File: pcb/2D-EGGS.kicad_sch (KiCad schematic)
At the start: 55 parts, among them J1 ISP, J10 B10, J11 B8, J12 PWAN_CENTER_LED, J13 PWAN_E1P1, J14 PWAN_E1P2, J15 ENCODER1, J16 DPWR, J17 PWAN_E2P1, J18 PWAN_E2P2, J19 ENCODER2, J2 TT_LED, J20 B9, J21 B11, J22 PWAN_USB_B, J23 PWAN_USB_C, J24 LED1, J25 LED2, J26 APWR, J3 B1, J4 B6, J5 B3, J6 B4, J7 B5, J8 B2, J9 B7, P1 USB_C_DATA, P2 USB_C_POWER, Q10 2N7002, Q11 2N7002, Q12 2N7002, Q13 2N7002, Q3 2N7002, Q4 2N7002, Q5 2N7002, Q6 2N7002, Q7 2N7002, Q8 2N7002, Q9 2N7002, SW1 SW_Push, U1 AT90USB1286, Y1 16MHz

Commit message: v3 routed
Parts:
- removed P1: USB_C_DATA, Connector_USB:USB_C_Receptacle_GCT_USB4085, symbol Connector:USB_C_Plug
- removed P2: USB_C_POWER, Connector_USB:USB_C_Receptacle_GCT_USB4085, symbol Connector:USB_C_Plug
- added J27: USB_DATA, Connector_JST:JST_XH_B4B-XH-A_1x04_P2.50mm_Vertical, symbol Connector_Generic:Conn_01x04
- added J28: USB_AUX, Connector_JST:JST_XH_B4B-XH-A_1x04_P2.50mm_Vertical, symbol Connector_Generic:Conn_01x04
- J1: footprint Connector_PinHeader_2.54mm:PinHeader_2x03_P2.54mm_Vertical -> Connector_IDC:IDC-Header_2x03_P2.54mm_Vertical
- J12: value PWAN_CENTER_LED -> DAO_BAR
- J13: value PWAN_E1P1 -> DAO_E1P1
- J14: value PWAN_E1P2 -> DAO_E1P2
- J17: value PWAN_E2P1 -> DAO_E2P1
- J18: value PWAN_E2P2 -> DAO_E2P2
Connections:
- net +5V: now also J27.4 (Pin_4); no longer J12.2 (Pin_2), J2.2 (Pin_2), J23.2 (Pin_2), J24.2 (Pin_2), J25.2 (Pin_2), J26.1 (Pin_1)
- net GND: now also J27.1 (Pin_1), J28.1 (Pin_1)
- net USB-R_D+: now also J27.2 (Pin_2)
- net USB-R_D-: now also J27.3 (Pin_3)
- new net +5VA: J12.2 (Pin_2), J2.2 (Pin_2), J23.2 (Pin_2), J24.2 (Pin_2), J25.2 (Pin_2), J26.1 (Pin_1), J28.4 (Pin_4)
- no-connect marks 43 -> 19

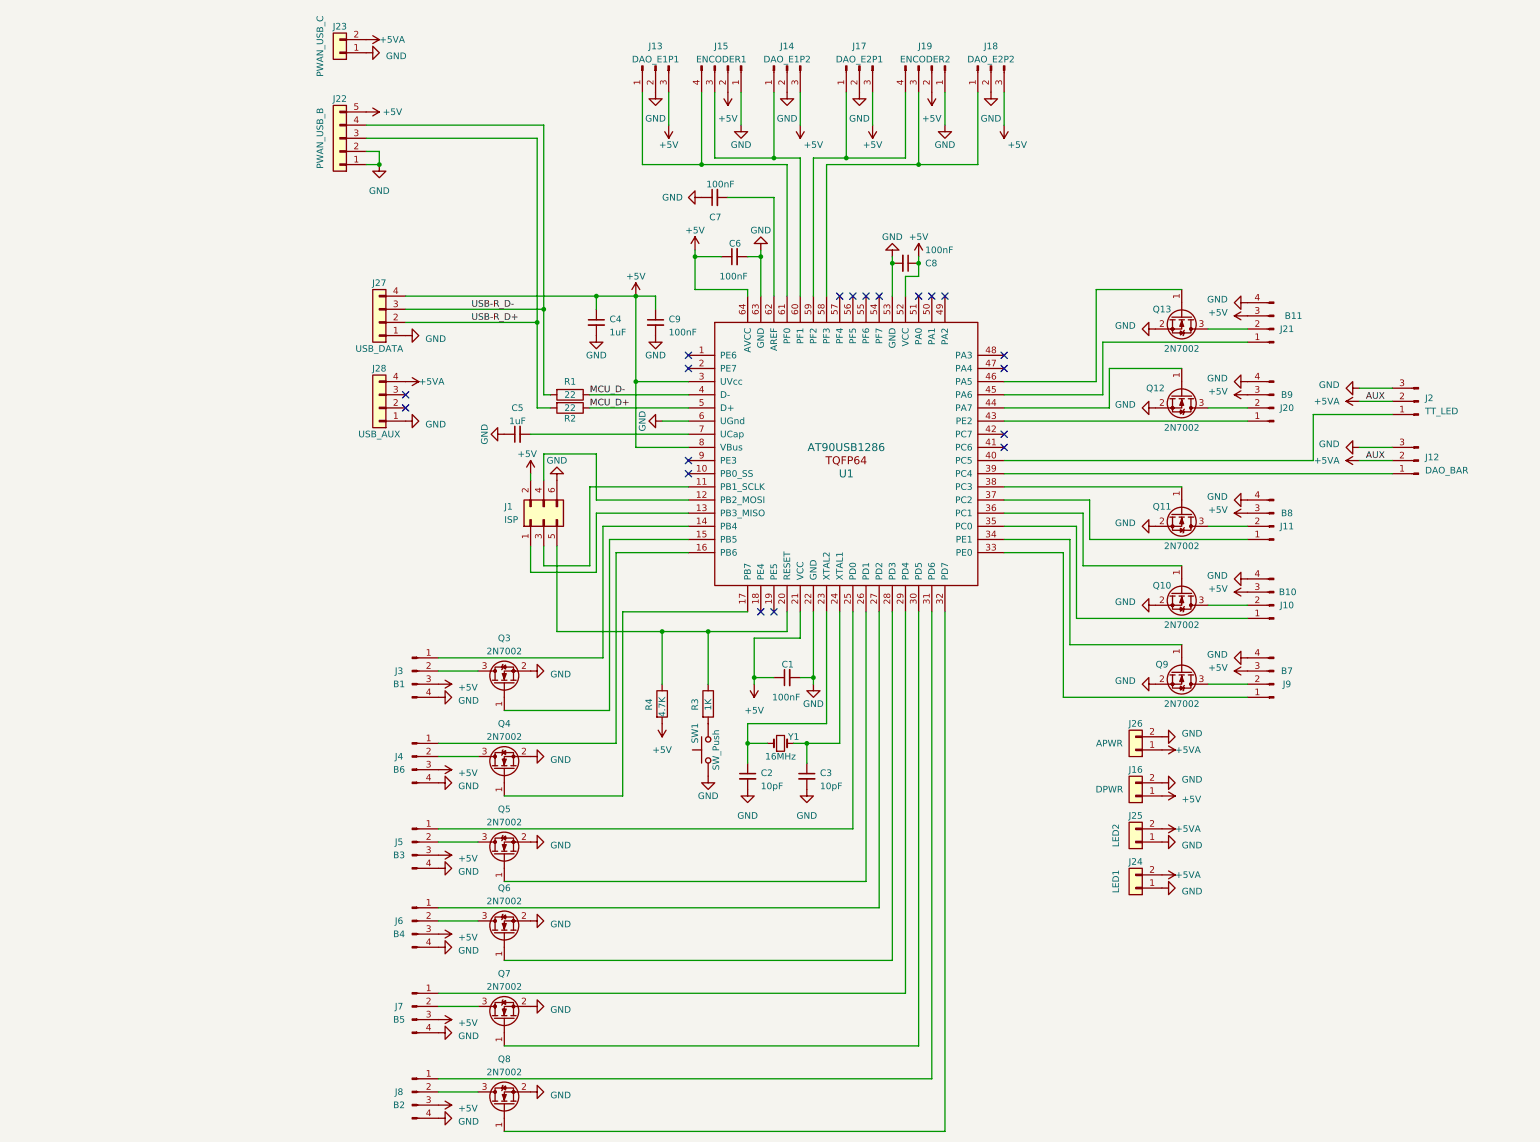
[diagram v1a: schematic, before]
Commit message: finalize V3
reduced JST-XH holes from 0.95mm -> 0.9mm, minor changes to layout
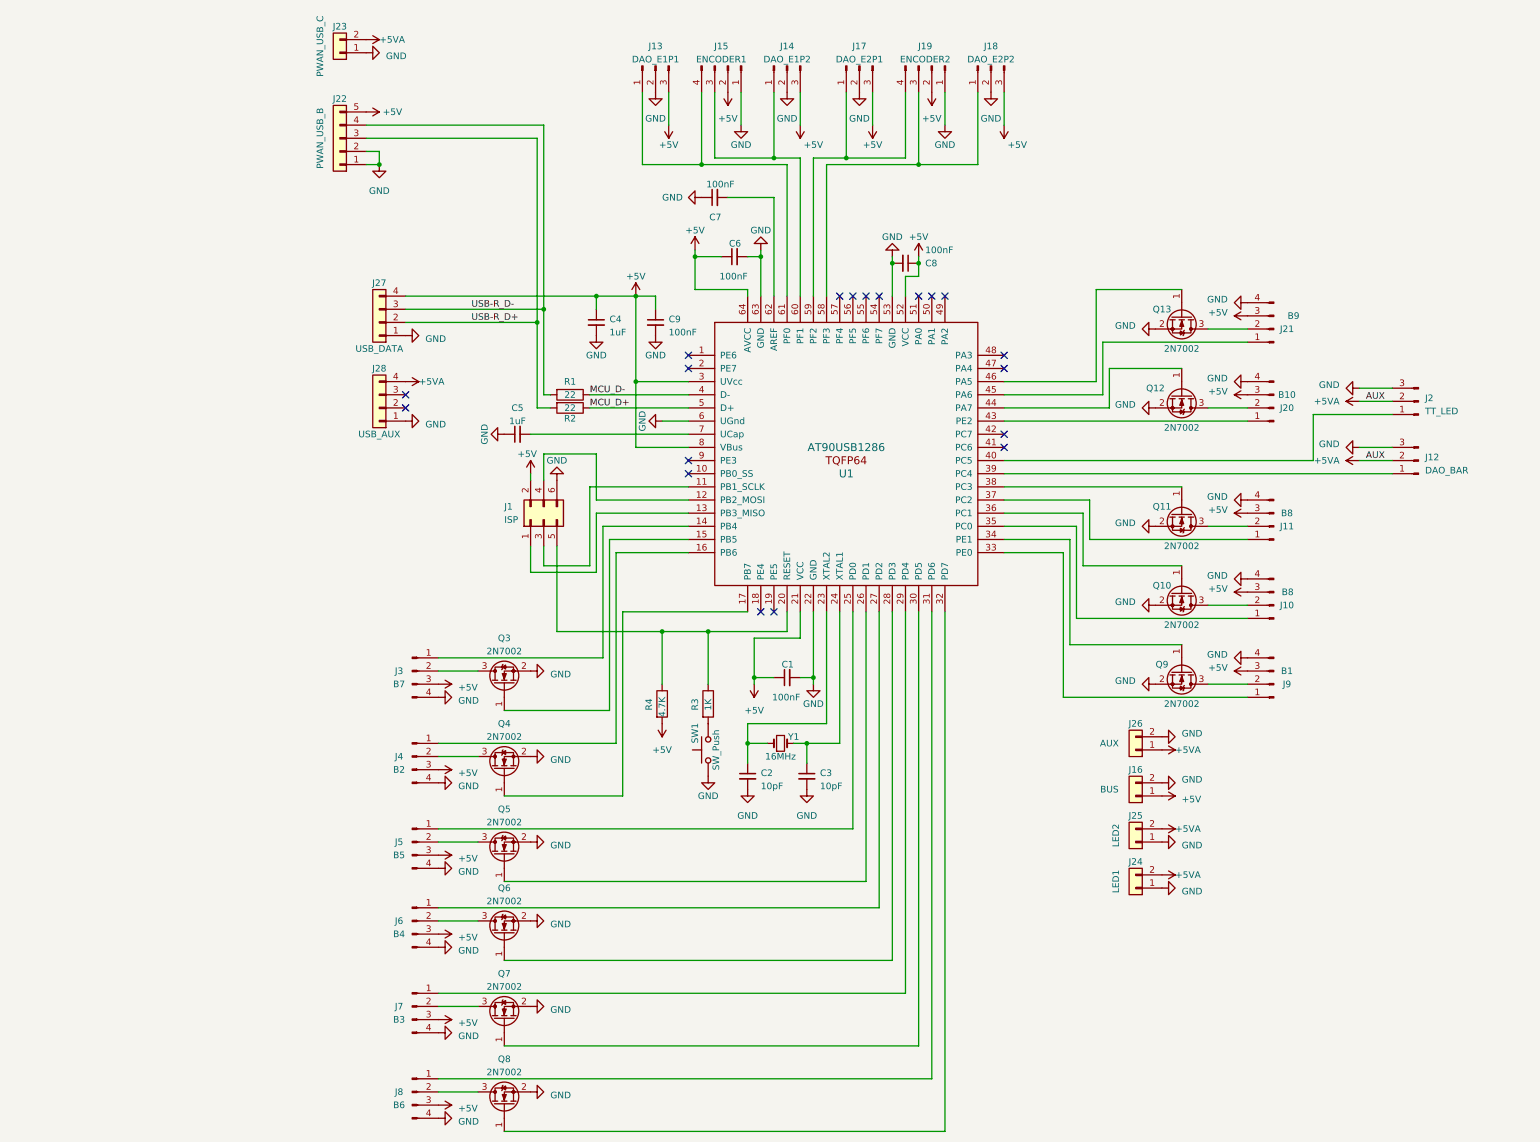
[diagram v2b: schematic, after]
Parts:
- J10: value B10 -> B8; footprint Connector_JST:JST_XH_B4B-XH-A_1x04_P2.50mm_Vertical -> BEEF-BOARD:JST_XH_B4B-XH-A_1x04_P2.50mm_Vertical_0.9mm_holes
- J11, J15, J19, J27, J28, J6: footprint Connector_JST:JST_XH_B4B-XH-A_1x04_P2.50mm_Vertical -> BEEF-BOARD:JST_XH_B4B-XH-A_1x04_P2.50mm_Vertical_0.9mm_holes
- J12, J13, J14, J17, J18, J2: footprint Connector_JST:JST_XH_B3B-XH-A_1x03_P2.50mm_Vertical -> BEEF-BOARD:JST_XH_B3B-XH-A_1x03_P2.50mm_Vertical_0.9mm_holes
- J16: value DPWR -> BUS
- J20: value B9 -> B10; footprint Connector_JST:JST_XH_B4B-XH-A_1x04_P2.50mm_Vertical -> BEEF-BOARD:JST_XH_B4B-XH-A_1x04_P2.50mm_Vertical_0.9mm_holes
- J21: value B11 -> B9; footprint Connector_JST:JST_XH_B4B-XH-A_1x04_P2.50mm_Vertical -> BEEF-BOARD:JST_XH_B4B-XH-A_1x04_P2.50mm_Vertical_0.9mm_holes
- J22: footprint Connector_JST:JST_XH_B5B-XH-A_1x05_P2.50mm_Vertical -> BEEF-BOARD:JST_XH_B5B-XH-A_1x05_P2.50mm_Vertical_0.9mm_holes
- J24, J25: footprint Connector_JST:JST_XH_B2B-XH-A_1x02_P2.50mm_Vertical -> BEEF-BOARD:JST_XH_B2B-XH-A_1x02_P2.50mm_Vertical_0.95mm_hole
- J26: value APWR -> AUX
- J3: value B1 -> B7; footprint Connector_JST:JST_XH_B4B-XH-A_1x04_P2.50mm_Vertical -> BEEF-BOARD:JST_XH_B4B-XH-A_1x04_P2.50mm_Vertical_0.9mm_holes
- J4: value B6 -> B2; footprint Connector_JST:JST_XH_B4B-XH-A_1x04_P2.50mm_Vertical -> BEEF-BOARD:JST_XH_B4B-XH-A_1x04_P2.50mm_Vertical_0.9mm_holes
- J5: value B3 -> B5; footprint Connector_JST:JST_XH_B4B-XH-A_1x04_P2.50mm_Vertical -> BEEF-BOARD:JST_XH_B4B-XH-A_1x04_P2.50mm_Vertical_0.9mm_holes
- J7: value B5 -> B3; footprint Connector_JST:JST_XH_B4B-XH-A_1x04_P2.50mm_Vertical -> BEEF-BOARD:JST_XH_B4B-XH-A_1x04_P2.50mm_Vertical_0.9mm_holes
- J8: value B2 -> B6; footprint Connector_JST:JST_XH_B4B-XH-A_1x04_P2.50mm_Vertical -> BEEF-BOARD:JST_XH_B4B-XH-A_1x04_P2.50mm_Vertical_0.9mm_holes
- J9: value B7 -> B1; footprint Connector_JST:JST_XH_B4B-XH-A_1x04_P2.50mm_Vertical -> BEEF-BOARD:JST_XH_B4B-XH-A_1x04_P2.50mm_Vertical_0.9mm_holes
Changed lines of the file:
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@@
       (effects (font (size 1.27 1.27)))
     )
-    (property "Value" "B5" (at 100.33 241.3 0)
+    (property "Value" "B3" (at 100.33 241.3 0)
       (effects (font (size 1.27 1.27)))
     )
-    (property "Footprint" "Connector_JST:JST_XH_B4B-XH-A_1x04_P2.50mm_Vertical" (at 102.87 238.76 0)
+    (property "Footprint" "BEEF-BOARD:JST_XH_B4B-XH-A_1x04_P2.50mm_Vertical_0.9mm_holes" (at 102.87 238.76 0)
       (effects (font (size 1.27 1.27)) hide)
     )
@@
       (effects (font (size 1.27 1.27)))
     )
-    (property "Footprint" "Connector_JST:JST_XH_B4B-XH-A_1x04_P2.50mm_Vertical" (at 102.87 222.25 0)
+    (property "Footprint" "BEEF-BOARD:JST_XH_B4B-XH-A_1x04_P2.50mm_Vertical_0.9mm_holes" (at 102.87 222.25 0)
       (effects (font (size 1.27 1.27)) hide)
     )
@@
       (effects (font (size 1.27 1.27)))
     )
-    (property "Footprint" "Connector_JST:JST_XH_B4B-XH-A_1x04_P2.50mm_Vertical" (at 96.52 106.68 0)
+    (property "Footprint" "BEEF-BOARD:JST_XH_B4B-XH-A_1x04_P2.50mm_Vertical_0.9mm_holes" (at 96.52 106.68 0)
       (effects (font (size 1.27 1.27)) hide)
     )
@@
       (effects (font (size 1.27 1.27)))
     )
-    (property "Value" "B9" (at 271.78 120.65 0)
+    (property "Value" "B10" (at 271.78 120.65 0)
       (effects (font (size 1.27 1.27)))
     )
-    (property "Footprint" "Connector_JST:JST_XH_B4B-XH-A_1x04_P2.50mm_Vertical" (at 269.24 123.19 0)
+    (property "Footprint" "BEEF-BOARD:JST_XH_B4B-XH-A_1x04_P2.50mm_Vertical_0.9mm_holes" (at 269.24 123.19 0)
       (effects (font (size 1.27 1.27)) hide)
     )
@@
       (effects (font (size 1.27 1.27)))
     )
-    (property "Value" "B1" (at 100.33 176.53 0)
+    (property "Value" "B7" (at 100.33 176.53 0)
       (effects (font (size 1.27 1.27)))
     )
-    (property "Footprint" "Connector_JST:JST_XH_B4B-XH-A_1x04_P2.50mm_Vertical" (at 102.87 173.99 0)
+    (property "Footprint" "BEEF-BOARD:JST_XH_B4B-XH-A_1x04_P2.50mm_Vertical_0.9mm_holes" (at 102.87 173.99 0)
       (effects (font (size 1.27 1.27)) hide)
     )
@@
       (effects (font (size 1.27 1.27)))
     )
-    (property "Footprint" "Connector_JST:JST_XH_B3B-XH-A_1x03_P2.50mm_Vertical" (at 149.86 57.15 0)
+    (property "Footprint" "BEEF-BOARD:JST_XH_B3B-XH-A_1x03_P2.50mm_Vertical_0.9mm_holes" (at 149.86 57.15 0)
       (effects (font (size 1.27 1.27)) hide)
     )
@@
       (effects (font (size 1.27 1.27)))
     )
-    (property "Value" "B6" (at 100.33 193.04 0)
+    (property "Value" "B2" (at 100.33 193.04 0)
       (effects (font (size 1.27 1.27)))
     )
-    (property "Footprint" "Connector_JST:JST_XH_B4B-XH-A_1x04_P2.50mm_Vertical" (at 102.87 190.5 0)
+    (property "Footprint" "BEEF-BOARD:JST_XH_B4B-XH-A_1x04_P2.50mm_Vertical_0.9mm_holes" (at 102.87 190.5 0)
       (effects (font (size 1.27 1.27)) hide)
     )
@@
       (effects (font (size 1.27 1.27)))
     )
-    (property "Footprint" "Connector_JST:JST_XH_B4B-XH-A_1x04_P2.50mm_Vertical" (at 163.83 57.15 0)
+    (property "Footprint" "BEEF-BOARD:JST_XH_B4B-XH-A_1x04_P2.50mm_Vertical_0.9mm_holes" (at 163.83 57.15 0)
       (effects (font (size 1.27 1.27)) hide)
     )
@@
       (effects (font (size 1.27 1.27)))
     )
-    (property "Footprint" "Connector_JST:JST_XH_B4B-XH-A_1x04_P2.50mm_Vertical" (at 96.52 123.19 0)
+    (property "Footprint" "BEEF-BOARD:JST_XH_B4B-XH-A_1x04_P2.50mm_Vertical_0.9mm_holes" (at 96.52 123.19 0)
       (effects (font (size 1.27 1.27)) hide)
     )
@@
       (effects (font (size 1.27 1.27)))
     )
-    (property "Value" "B7" (at 271.78 173.99 0)
+    (property "Value" "B1" (at 271.78 173.99 0)
       (effects (font (size 1.27 1.27)))
     )
-    (property "Footprint" "Connector_JST:JST_XH_B4B-XH-A_1x04_P2.50mm_Vertical" (at 269.24 176.53 0)
+    (property "Footprint" "BEEF-BOARD:JST_XH_B4B-XH-A_1x04_P2.50mm_Vertical_0.9mm_holes" (at 269.24 176.53 0)
       (effects (font (size 1.27 1.27)) hide)
     )
@@
       (effects (font (size 1.27 1.27)) (justify right))
     )
-    (property "Footprint" "Connector_JST:JST_XH_B3B-XH-A_1x03_P2.50mm_Vertical" (at 297.18 133.35 0)
+    (property "Footprint" "BEEF-BOARD:JST_XH_B3B-XH-A_1x03_P2.50mm_Vertical_0.9mm_holes" (at 297.18 133.35 0)
       (effects (font (size 1.27 1.27)) hide)
     )
@@
       (effects (font (size 1.27 1.27)))
     )
-    (property "Footprint" "Connector_JST:JST_XH_B5B-XH-A_1x05_P2.50mm_Vertical" (at 88.9 71.12 0)
+    (property "Footprint" "BEEF-BOARD:JST_XH_B5B-XH-A_1x05_P2.50mm_Vertical_0.9mm_holes" (at 88.9 71.12 0)
       (effects (font (size 1.27 1.27)) hide)
     )
@@
       (effects (font (size 1.27 1.27)))
     )
-    (property "Footprint" "Connector_JST:JST_XH_B3B-XH-A_1x03_P2.50mm_Vertical" (at 189.23 57.15 0)
+    (property "Footprint" "BEEF-BOARD:JST_XH_B3B-XH-A_1x03_P2.50mm_Vertical_0.9mm_holes" (at 189.23 57.15 0)
       (effects (font (size 1.27 1.27)) hide)
     )
@@
       (effects (font (size 1.27 1.27)))
     )
-    (property "Value" "B11" (at 273.05 105.41 0)
+    (property "Value" "B9" (at 273.05 105.41 0)
       (effects (font (size 1.27 1.27)))
     )
-    (property "Footprint" "Connector_JST:JST_XH_B4B-XH-A_1x04_P2.50mm_Vertical" (at 269.24 107.95 0)
+    (property "Footprint" "BEEF-BOARD:JST_XH_B4B-XH-A_1x04_P2.50mm_Vertical_0.9mm_holes" (at 269.24 107.95 0)
       (effects (font (size 1.27 1.27)) hide)
     )
@@
       (effects (font (size 1.27 1.27)))
     )
-    (property "Value" "APWR" (at 237.49 187.96 0)
+    (property "Value" "AUX" (at 237.49 187.96 0)
       (effects (font (size 1.27 1.27)))
     )
@@
       (effects (font (size 1.27 1.27)) (justify right))
     )
-    (property "Footprint" "Connector_JST:JST_XH_B3B-XH-A_1x03_P2.50mm_Vertical" (at 297.18 121.92 0)
+    (property "Footprint" "BEEF-BOARD:JST_XH_B3B-XH-A_1x03_P2.50mm_Vertical_0.9mm_holes" (at 297.18 121.92 0)
       (effects (font (size 1.27 1.27)) hide)
     )
@@
       (effects (font (size 1.27 1.27)))
     )
-    (property "Footprint" "Connector_JST:JST_XH_B3B-XH-A_1x03_P2.50mm_Vertical" (at 175.26 57.15 0)
+    (property "Footprint" "BEEF-BOARD:JST_XH_B3B-XH-A_1x03_P2.50mm_Vertical_0.9mm_holes" (at 175.26 57.15 0)
       (effects (font (size 1.27 1.27)) hide)
     )
@@
       (effects (font (size 1.27 1.27)))
     )
-    (property "Footprint" "Connector_JST:JST_XH_B4B-XH-A_1x04_P2.50mm_Vertical" (at 269.24 146.05 0)
+    (property "Footprint" "BEEF-BOARD:JST_XH_B4B-XH-A_1x04_P2.50mm_Vertical_0.9mm_holes" (at 269.24 146.05 0)
       (effects (font (size 1.27 1.27)) hide)
     )
@@
       (effects (font (size 1.27 1.27)))
     )
-    (property "Footprint" "Connector_JST:JST_XH_B2B-XH-A_1x02_P2.50mm_Vertical" (at 242.57 207.01 0)
+    (property "Footprint" "BEEF-BOARD:JST_XH_B2B-XH-A_1x02_P2.50mm_Vertical_0.95mm_hole" (at 242.57 207.01 0)
       (effects (font (size 1.27 1.27)) hide)
     )
@@
       (effects (font (size 1.27 1.27)))
     )
-    (property "Footprint" "Connector_JST:JST_XH_B2B-XH-A_1x02_P2.50mm_Vertical" (at 242.57 215.9 0)
+    (property "Footprint" "BEEF-BOARD:JST_XH_B2B-XH-A_1x02_P2.50mm_Vertical_0.95mm_hole" (at 242.57 215.9 0)
       (effects (font (size 1.27 1.27)) hide)
     )
@@
       (effects (font (size 1.27 1.27)))
     )
-    (property "Footprint" "Connector_JST:JST_XH_B4B-XH-A_1x04_P2.50mm_Vertical" (at 203.2 57.15 0)
+    (property "Footprint" "BEEF-BOARD:JST_XH_B4B-XH-A_1x04_P2.50mm_Vertical_0.9mm_holes" (at 203.2 57.15 0)
       (effects (font (size 1.27 1.27)) hide)
     )
@@
       (effects (font (size 1.27 1.27)))
     )
-    (property "Value" "DPWR" (at 237.49 196.85 0)
+    (property "Value" "BUS" (at 237.49 196.85 0)
       (effects (font (size 1.27 1.27)))
     )
@@
       (effects (font (size 1.27 1.27)))
     )
-    (property "Value" "B3" (at 100.33 209.55 0)
+    (property "Value" "B5" (at 100.33 209.55 0)
       (effects (font (size 1.27 1.27)))
     )
-    (property "Footprint" "Connector_JST:JST_XH_B4B-XH-A_1x04_P2.50mm_Vertical" (at 102.87 207.01 0)
+    (property "Footprint" "BEEF-BOARD:JST_XH_B4B-XH-A_1x04_P2.50mm_Vertical_0.9mm_holes" (at 102.87 207.01 0)
       (effects (font (size 1.27 1.27)) hide)
     )
@@
       (effects (font (size 1.27 1.27)))
     )
-    (property "Value" "B2" (at 100.33 257.81 0)
+    (property "Value" "B6" (at 100.33 257.81 0)
       (effects (font (size 1.27 1.27)))
     )
-    (property "Footprint" "Connector_JST:JST_XH_B4B-XH-A_1x04_P2.50mm_Vertical" (at 102.87 255.27 0)
+    (property "Footprint" "BEEF-BOARD:JST_XH_B4B-XH-A_1x04_P2.50mm_Vertical_0.9mm_holes" (at 102.87 255.27 0)
       (effects (font (size 1.27 1.27)) hide)
     )
@@
       (effects (font (size 1.27 1.27)))
     )
-    (property "Value" "B10" (at 271.916 158.75 0)
+    (property "Value" "B8" (at 271.916 158.75 0)
       (effects (font (size 1.27 1.27)))
     )
-    (property "Footprint" "Connector_JST:JST_XH_B4B-XH-A_1x04_P2.50mm_Vertical" (at 269.24 161.29 0)
+    (property "Footprint" "BEEF-BOARD:JST_XH_B4B-XH-A_1x04_P2.50mm_Vertical_0.9mm_holes" (at 269.24 161.29 0)
       (effects (font (size 1.27 1.27)) hide)
     )
@@
       (effects (font (size 1.27 1.27)))
     )
-    (property "Footprint" "Connector_JST:JST_XH_B3B-XH-A_1x03_P2.50mm_Vertical" (at 214.63 57.15 0)
+    (property "Footprint" "BEEF-BOARD:JST_XH_B3B-XH-A_1x03_P2.50mm_Vertical_0.9mm_holes" (at 214.63 57.15 0)
       (effects (font (size 1.27 1.27)) hide)
     )
